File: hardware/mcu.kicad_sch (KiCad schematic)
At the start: 56 parts, among them J10 PRPC001DAAN-RC, J11 PRPC006SAAN-RC, J12 PRPC004SAAN-RC, J8 SBH11-NBPC-D05-SM-BK, J9 PRPC006SAAN-RC, U5 AT25SF081B-SSHD-B, U6 MCP9808, U7 STM32L552CETx, Y1 ABS05-32.768KHZ-9-T, Y2 ECS-160-9-37-CKM-TR3

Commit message: HW: Fix components
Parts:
- renumbered R11 to R12, R12 to R13, R13 to R14, R14 to R15, R15 to R16, R16 to R17, R17 to R18, R18 to R19, R19 to R20, R20 to R21, R21 to R22, R22 to R23, R23 to R24, R24 to R25, R25 to R26, R26 to R27
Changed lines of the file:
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@@
 		(on_board yes)
 		(dnp yes)
-		(property "Reference" "R20"
+		(property "Reference" "R21"
 			(at 222.504 144.78 0)
 			(effects
@@
 			(project "iida_devkit"
 				(path "/b12a6e25-97fb-4aba-bc96-af8db389bb9a/6dd8d741-3080-458c-a4f5-a05a3905bb8a"
-					(reference "R20")
+					(reference "R21")
 					(unit 1)
 				)
@@
 		(on_board yes)
 		(dnp no)
-		(property "Reference" "R12"
+		(property "Reference" "R13"
 			(at 104.394 104.394 90)
 			(effects
@@
 			(project "iida_devkit"
 				(path "/b12a6e25-97fb-4aba-bc96-af8db389bb9a/6dd8d741-3080-458c-a4f5-a05a3905bb8a"
-					(reference "R12")
+					(reference "R13")
 					(unit 1)
 				)
@@
 		(on_board yes)
 		(dnp no)
-		(property "Reference" "R21"
+		(property "Reference" "R22"
 			(at 222.504 154.94 0)
 			(effects
@@
 			(project "iida_devkit"
 				(path "/b12a6e25-97fb-4aba-bc96-af8db389bb9a/6dd8d741-3080-458c-a4f5-a05a3905bb8a"
-					(reference "R21")
+					(reference "R22")
 					(unit 1)
 				)
@@
 		(on_board yes)
 		(dnp no)
-		(property "Reference" "R17"
+		(property "Reference" "R18"
 			(at 185.166 66.294 90)
 			(effects
@@
 			(project "iida_devkit"
 				(path "/b12a6e25-97fb-4aba-bc96-af8db389bb9a/6dd8d741-3080-458c-a4f5-a05a3905bb8a"
-					(reference "R17")
+					(reference "R18")
 					(unit 1)
 				)
@@
 		(on_board yes)
 		(dnp no)
-		(property "Reference" "R13"
+		(property "Reference" "R14"
 			(at 106.426 106.68 90)
 			(effects
@@
 			(project "iida_devkit"
 				(path "/b12a6e25-97fb-4aba-bc96-af8db389bb9a/6dd8d741-3080-458c-a4f5-a05a3905bb8a"
-					(reference "R13")
+					(reference "R14")
 					(unit 1)
 				)
@@
 		(on_board yes)
 		(dnp no)
-		(property "Reference" "R25"
+		(property "Reference" "R26"
 			(at 260.604 26.924 90)
 			(effects
@@
 			(project "iida_devkit"
 				(path "/b12a6e25-97fb-4aba-bc96-af8db389bb9a/6dd8d741-3080-458c-a4f5-a05a3905bb8a"
-					(reference "R25")
+					(reference "R26")
 					(unit 1)
 				)
@@
 		(on_board yes)
 		(dnp no)
-		(property "Reference" "R11"
+		(property "Reference" "R12"
 			(at 104.394 101.854 90)
 			(effects
@@
 			(project ""
 				(path "/b12a6e25-97fb-4aba-bc96-af8db389bb9a/6dd8d741-3080-458c-a4f5-a05a3905bb8a"
-					(reference "R11")
+					(reference "R12")
 					(unit 1)
 				)
@@
 		(on_board yes)
 		(dnp no)
-		(property "Reference" "R14"
+		(property "Reference" "R15"
 			(at 106.426 109.22 90)
 			(effects
@@
 			(project "iida_devkit"
 				(path "/b12a6e25-97fb-4aba-bc96-af8db389bb9a/6dd8d741-3080-458c-a4f5-a05a3905bb8a"
-					(reference "R14")
+					(reference "R15")
 					(unit 1)
 				)
@@
 		(on_board yes)
 		(dnp no)
-		(property "Reference" "R24"
+		(property "Reference" "R25"
 			(at 260.604 23.114 90)
 			(effects
@@
 			(project "iida_devkit"
 				(path "/b12a6e25-97fb-4aba-bc96-af8db389bb9a/6dd8d741-3080-458c-a4f5-a05a3905bb8a"
-					(reference "R24")
+					(reference "R25")
 					(unit 1)
 				)
@@
 		(on_board yes)
 		(dnp no)
-		(property "Reference" "R15"
+		(property "Reference" "R16"
 			(at 106.426 119.634 90)
 			(effects
@@
 			(project "iida_devkit"
 				(path "/b12a6e25-97fb-4aba-bc96-af8db389bb9a/6dd8d741-3080-458c-a4f5-a05a3905bb8a"
-					(reference "R15")
+					(reference "R16")
 					(unit 1)
 				)
@@
 		(on_board yes)
 		(dnp no)
-		(property "Reference" "R16"
+		(property "Reference" "R17"
 			(at 106.426 122.174 90)
 			(effects
@@
 			(project "iida_devkit"
 				(path "/b12a6e25-97fb-4aba-bc96-af8db389bb9a/6dd8d741-3080-458c-a4f5-a05a3905bb8a"
-					(reference "R16")
+					(reference "R17")
 					(unit 1)
 				)
@@
 		(on_board yes)
 		(dnp yes)
-		(property "Reference" "R22"
+		(property "Reference" "R23"
 			(at 230.124 144.78 0)
 			(effects
@@
 			(project "iida_devkit"
 				(path "/b12a6e25-97fb-4aba-bc96-af8db389bb9a/6dd8d741-3080-458c-a4f5-a05a3905bb8a"
-					(reference "R22")
+					(reference "R23")
 					(unit 1)
 				)
@@
 		(on_board yes)
 		(dnp no)
-		(property "Reference" "R19"
+		(property "Reference" "R20"
 			(at 193.294 146.304 0)
 			(effects
@@
 			(project "iida_devkit"
 				(path "/b12a6e25-97fb-4aba-bc96-af8db389bb9a/6dd8d741-3080-458c-a4f5-a05a3905bb8a"
-					(reference "R19")
+					(reference "R20")
 					(unit 1)
 				)
@@
 		(on_board yes)
 		(dnp no)
-		(property "Reference" "R26"
+		(property "Reference" "R27"
 			(at 260.604 30.734 90)
 			(effects
@@
 			(project "iida_devkit"
 				(path "/b12a6e25-97fb-4aba-bc96-af8db389bb9a/6dd8d741-3080-458c-a4f5-a05a3905bb8a"
-					(reference "R26")
+					(reference "R27")
 					(unit 1)
 				)
@@
 		(on_board yes)
 		(dnp no)
-		(property "Reference" "R23"
+		(property "Reference" "R24"
 			(at 230.124 154.94 0)
 			(effects
@@
 			(project "iida_devkit"
 				(path "/b12a6e25-97fb-4aba-bc96-af8db389bb9a/6dd8d741-3080-458c-a4f5-a05a3905bb8a"
-					(reference "R23")
+					(reference "R24")
 					(unit 1)
 				)
@@
 		(on_board yes)
 		(dnp no)
-		(property "Reference" "R18"
+		(property "Reference" "R19"
 			(at 185.166 68.834 90)
 			(effects
@@
 			(project "iida_devkit"
 				(path "/b12a6e25-97fb-4aba-bc96-af8db389bb9a/6dd8d741-3080-458c-a4f5-a05a3905bb8a"
-					(reference "R18")
+					(reference "R19")
 					(unit 1)
 				)

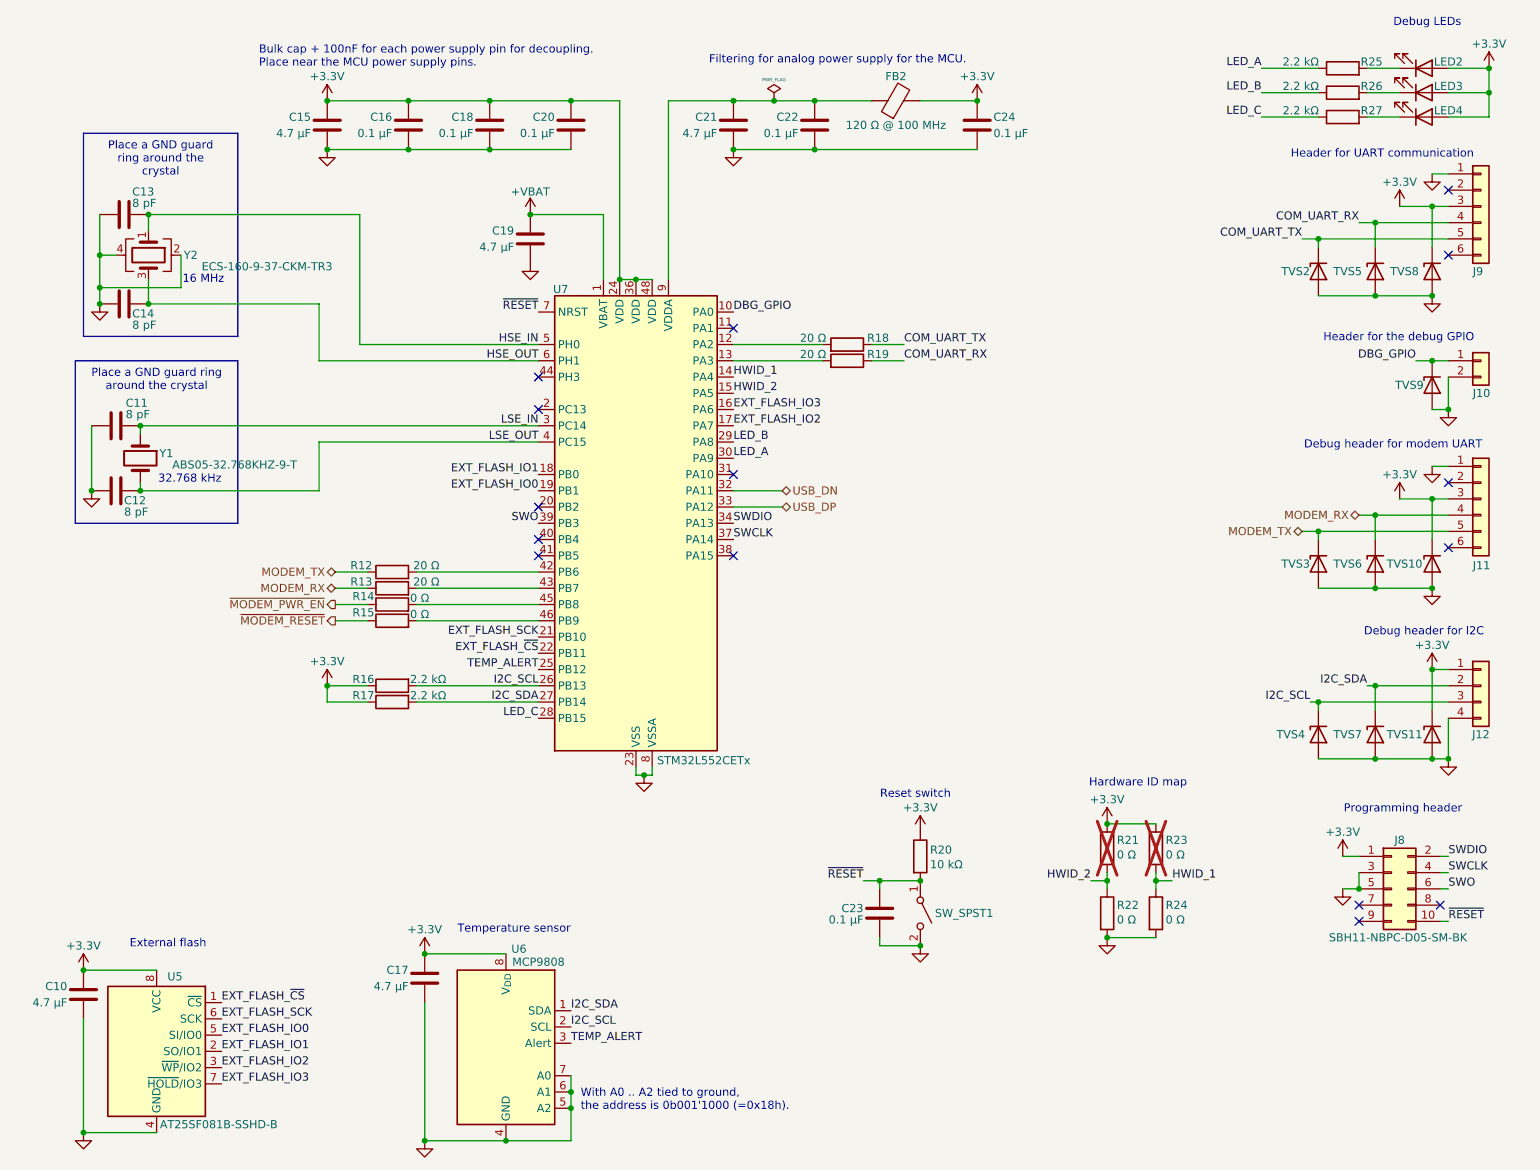
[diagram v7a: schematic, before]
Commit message: HW: Refine schema and layout based on review
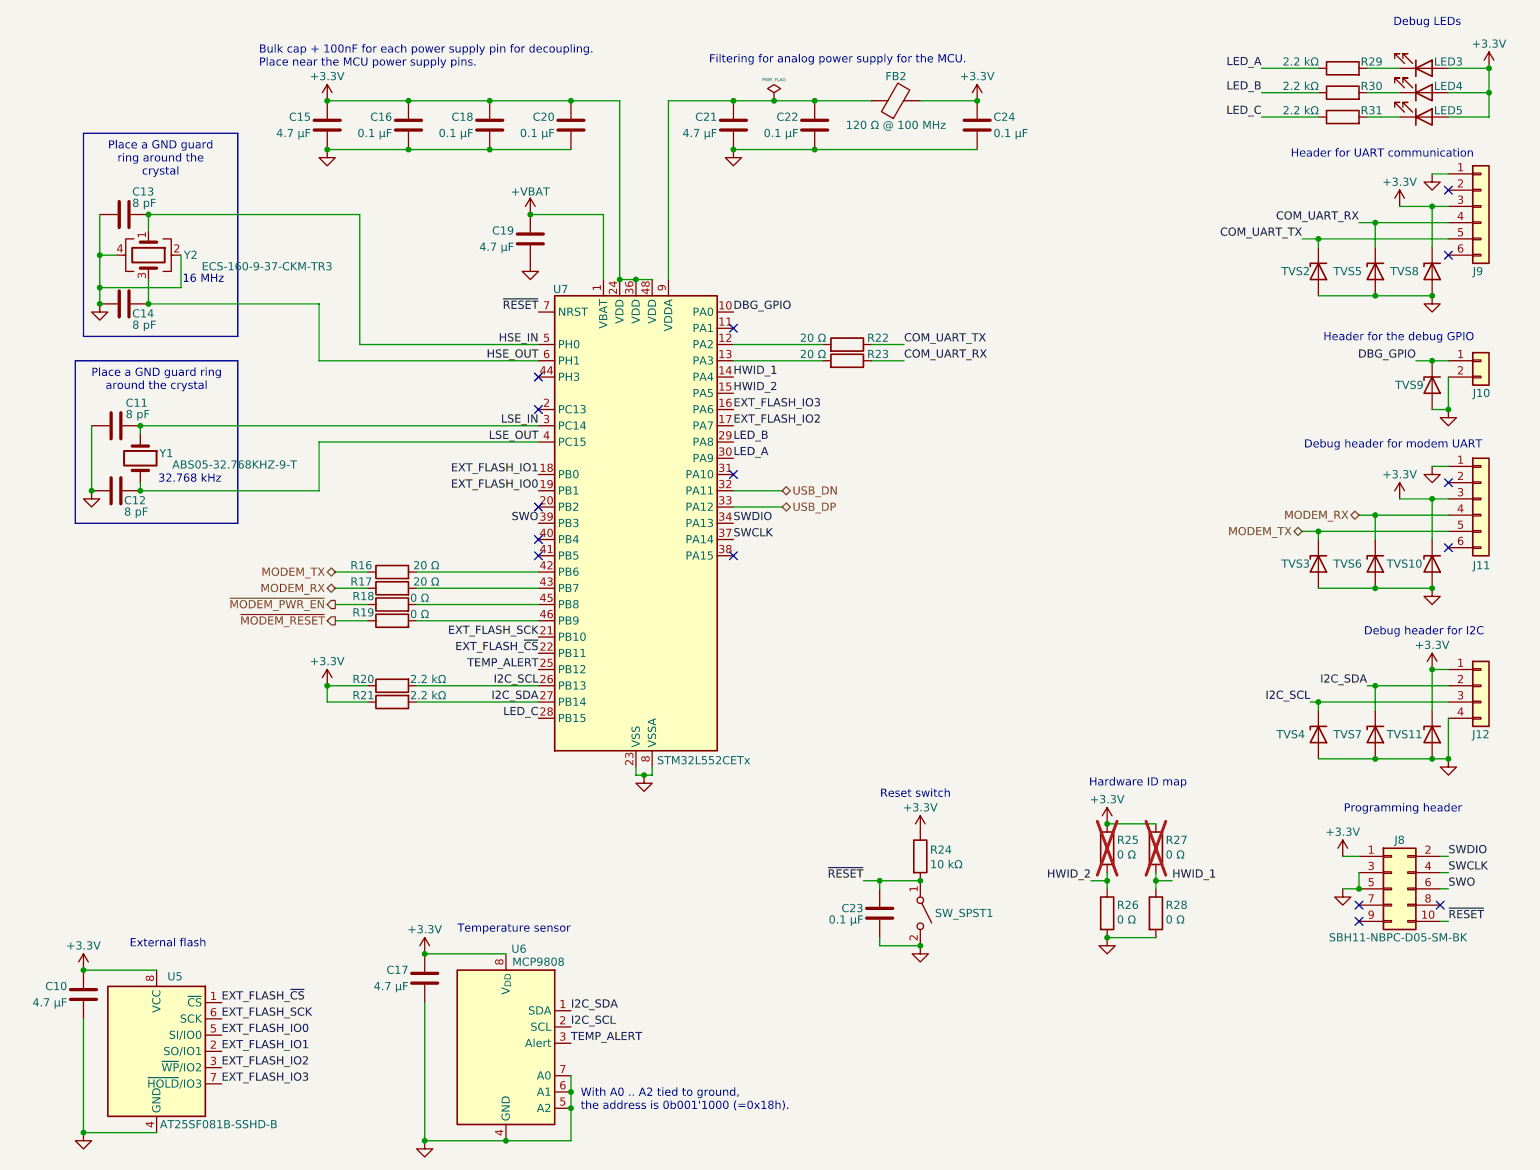
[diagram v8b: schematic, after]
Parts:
- renumbered LED2 to LED3, LED3 to LED4, LED4 to LED5, R12 to R16, R13 to R17, R14 to R18, R15 to R19, R16 to R20, R17 to R21, R18 to R22, R19 to R23, R20 to R24, R21 to R25, R22 to R26, R23 to R27, R24 to R28, R25 to R29, R26 to R30, R27 to R31
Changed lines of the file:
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@@
 		(on_board yes)
 		(dnp yes)
-		(property "Reference" "R21"
+		(property "Reference" "R25"
 			(at 222.504 144.78 0)
 			(effects
@@
 			(project "iida_devkit"
 				(path "/b12a6e25-97fb-4aba-bc96-af8db389bb9a/6dd8d741-3080-458c-a4f5-a05a3905bb8a"
-					(reference "R21")
+					(reference "R25")
 					(unit 1)
 				)
@@
 		(on_board yes)
 		(dnp no)
-		(property "Reference" "R13"
+		(property "Reference" "R17"
 			(at 104.394 104.394 90)
 			(effects
@@
 			(project "iida_devkit"
 				(path "/b12a6e25-97fb-4aba-bc96-af8db389bb9a/6dd8d741-3080-458c-a4f5-a05a3905bb8a"
-					(reference "R13")
+					(reference "R17")
 					(unit 1)
 				)
@@
 		(on_board yes)
 		(dnp no)
-		(property "Reference" "R22"
+		(property "Reference" "R26"
 			(at 222.504 154.94 0)
 			(effects
@@
 			(project "iida_devkit"
 				(path "/b12a6e25-97fb-4aba-bc96-af8db389bb9a/6dd8d741-3080-458c-a4f5-a05a3905bb8a"
-					(reference "R22")
+					(reference "R26")
 					(unit 1)
 				)
@@
 		(on_board yes)
 		(dnp no)
-		(property "Reference" "R18"
+		(property "Reference" "R22"
 			(at 185.166 66.294 90)
 			(effects
@@
 			(project "iida_devkit"
 				(path "/b12a6e25-97fb-4aba-bc96-af8db389bb9a/6dd8d741-3080-458c-a4f5-a05a3905bb8a"
-					(reference "R18")
+					(reference "R22")
 					(unit 1)
 				)
@@
 		(on_board yes)
 		(dnp no)
-		(property "Reference" "R14"
+		(property "Reference" "R18"
 			(at 106.426 106.68 90)
 			(effects
@@
 			(project "iida_devkit"
 				(path "/b12a6e25-97fb-4aba-bc96-af8db389bb9a/6dd8d741-3080-458c-a4f5-a05a3905bb8a"
-					(reference "R14")
+					(reference "R18")
 					(unit 1)
 				)
@@
 		(on_board yes)
 		(dnp no)
-		(property "Reference" "R26"
+		(property "Reference" "R30"
 			(at 260.604 26.924 90)
 			(effects
@@
 			(project "iida_devkit"
 				(path "/b12a6e25-97fb-4aba-bc96-af8db389bb9a/6dd8d741-3080-458c-a4f5-a05a3905bb8a"
-					(reference "R26")
+					(reference "R30")
 					(unit 1)
 				)
@@
 		(on_board yes)
 		(dnp no)
-		(property "Reference" "R12"
+		(property "Reference" "R16"
 			(at 104.394 101.854 90)
 			(effects
@@
 			(project ""
 				(path "/b12a6e25-97fb-4aba-bc96-af8db389bb9a/6dd8d741-3080-458c-a4f5-a05a3905bb8a"
-					(reference "R12")
+					(reference "R16")
 					(unit 1)
 				)
@@
 		(on_board yes)
 		(dnp no)
-		(property "Reference" "R15"
+		(property "Reference" "R19"
 			(at 106.426 109.22 90)
 			(effects
@@
 			(project "iida_devkit"
 				(path "/b12a6e25-97fb-4aba-bc96-af8db389bb9a/6dd8d741-3080-458c-a4f5-a05a3905bb8a"
-					(reference "R15")
+					(reference "R19")
 					(unit 1)
 				)
@@
 		(on_board yes)
 		(dnp no)
-		(property "Reference" "LED3"
+		(property "Reference" "LED4"
 			(at 274.32 26.924 0)
 			(effects
@@
 			(project "iida_devkit"
 				(path "/b12a6e25-97fb-4aba-bc96-af8db389bb9a/6dd8d741-3080-458c-a4f5-a05a3905bb8a"
-					(reference "LED3")
+					(reference "LED4")
 					(unit 1)
 				)
@@
 		(on_board yes)
 		(dnp no)
-		(property "Reference" "LED2"
+		(property "Reference" "LED3"
 			(at 274.32 23.114 0)
 			(effects
@@
 			(project "iida_devkit"
 				(path "/b12a6e25-97fb-4aba-bc96-af8db389bb9a/6dd8d741-3080-458c-a4f5-a05a3905bb8a"
-					(reference "LED2")
+					(reference "LED3")
 					(unit 1)
 				)
@@
 		(on_board yes)
 		(dnp no)
-		(property "Reference" "R25"
+		(property "Reference" "R29"
 			(at 260.604 23.114 90)
 			(effects
@@
 			(project "iida_devkit"
 				(path "/b12a6e25-97fb-4aba-bc96-af8db389bb9a/6dd8d741-3080-458c-a4f5-a05a3905bb8a"
-					(reference "R25")
+					(reference "R29")
 					(unit 1)
 				)
@@
 		(on_board yes)
 		(dnp no)
-		(property "Reference" "R16"
+		(property "Reference" "R20"
 			(at 106.426 119.634 90)
 			(effects
@@
 			(project "iida_devkit"
 				(path "/b12a6e25-97fb-4aba-bc96-af8db389bb9a/6dd8d741-3080-458c-a4f5-a05a3905bb8a"
-					(reference "R16")
+					(reference "R20")
 					(unit 1)
 				)
@@
 		(on_board yes)
 		(dnp no)
-		(property "Reference" "R17"
+		(property "Reference" "R21"
 			(at 106.426 122.174 90)
 			(effects
@@
 			(project "iida_devkit"
 				(path "/b12a6e25-97fb-4aba-bc96-af8db389bb9a/6dd8d741-3080-458c-a4f5-a05a3905bb8a"
-					(reference "R17")
+					(reference "R21")
 					(unit 1)
 				)
@@
 		(on_board yes)
 		(dnp yes)
-		(property "Reference" "R23"
+		(property "Reference" "R27"
 			(at 230.124 144.78 0)
 			(effects
@@
 			(project "iida_devkit"
 				(path "/b12a6e25-97fb-4aba-bc96-af8db389bb9a/6dd8d741-3080-458c-a4f5-a05a3905bb8a"
-					(reference "R23")
+					(reference "R27")
 					(unit 1)
 				)
@@
 		(on_board yes)
 		(dnp no)
-		(property "Reference" "R20"
+		(property "Reference" "R24"
 			(at 193.294 146.304 0)
 			(effects
@@
 			(project "iida_devkit"
 				(path "/b12a6e25-97fb-4aba-bc96-af8db389bb9a/6dd8d741-3080-458c-a4f5-a05a3905bb8a"
-					(reference "R20")
+					(reference "R24")
 					(unit 1)
 				)
@@
 		(on_board yes)
 		(dnp no)
-		(property "Reference" "R27"
+		(property "Reference" "R31"
 			(at 260.604 30.734 90)
 			(effects
@@
 			(project "iida_devkit"
 				(path "/b12a6e25-97fb-4aba-bc96-af8db389bb9a/6dd8d741-3080-458c-a4f5-a05a3905bb8a"
-					(reference "R27")
+					(reference "R31")
 					(unit 1)
 				)
@@
 		(on_board yes)
 		(dnp no)
-		(property "Reference" "LED4"
+		(property "Reference" "LED5"
 			(at 274.32 30.734 0)
 			(effects
@@
 			(project "iida_devkit"
 				(path "/b12a6e25-97fb-4aba-bc96-af8db389bb9a/6dd8d741-3080-458c-a4f5-a05a3905bb8a"
-					(reference "LED4")
+					(reference "LED5")
 					(unit 1)
 				)
@@
 		(on_board yes)
 		(dnp no)
-		(property "Reference" "R24"
+		(property "Reference" "R28"
 			(at 230.124 154.94 0)
 			(effects
@@
 			(project "iida_devkit"
 				(path "/b12a6e25-97fb-4aba-bc96-af8db389bb9a/6dd8d741-3080-458c-a4f5-a05a3905bb8a"
-					(reference "R24")
+					(reference "R28")
 					(unit 1)
 				)
@@
 		(on_board yes)
 		(dnp no)
-		(property "Reference" "R19"
+		(property "Reference" "R23"
 			(at 185.166 68.834 90)
 			(effects
@@
 			(project "iida_devkit"
 				(path "/b12a6e25-97fb-4aba-bc96-af8db389bb9a/6dd8d741-3080-458c-a4f5-a05a3905bb8a"
-					(reference "R19")
+					(reference "R23")
 					(unit 1)
 				)
